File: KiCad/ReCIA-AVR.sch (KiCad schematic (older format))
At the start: 26 parts, among them U1 AVR128DA64-I_MR, U2 74AHCT1G17, U3 TLC2932AIPWR, U5 8520_DIP

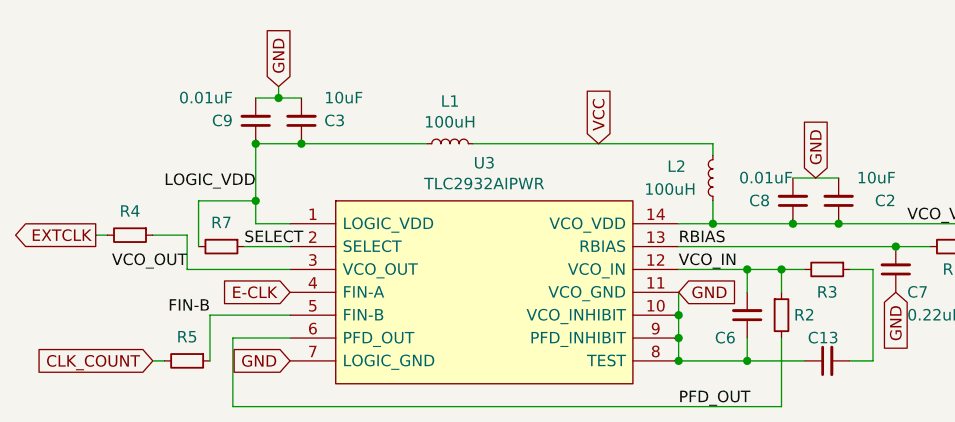
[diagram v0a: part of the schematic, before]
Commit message: corrected C8,C9 to 0.1uF
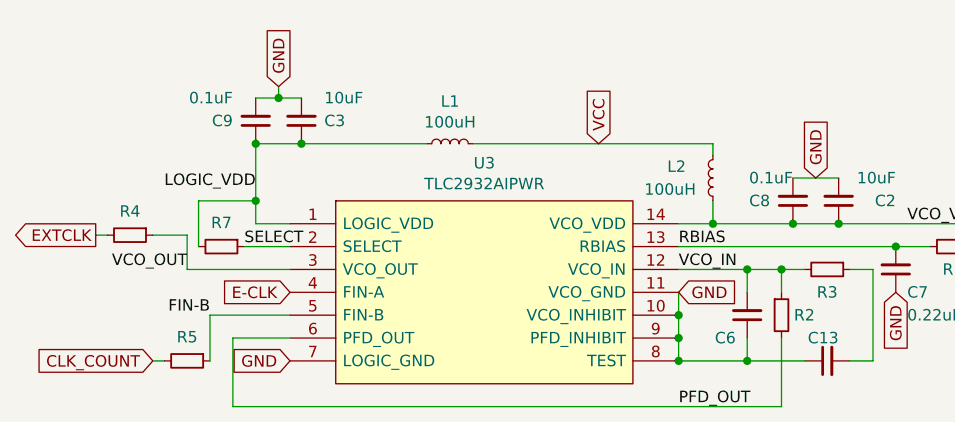
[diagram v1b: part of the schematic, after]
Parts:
- C8, C9: value 0.01uF -> 0.1uF
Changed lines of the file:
@@
 P 7650 1100
 F 0 "C9" H 7750 1100 50  0000 L CNN
-F 1 "0.01uF" H 7750 1000 50  0000 L CNN
+F 1 "0.1uF" H 7750 1000 50  0000 L CNN
 F 2 "Capacitor_SMD:C_0603_1608Metric_Pad1.08x0.95mm_HandSolder" H 7650 1100 50  0001 C CNN
 F 3 "~" H 7650 1100 50  0001 C CNN
@@
 P 10000 1450
 F 0 "C8" H 10100 1450 50  0000 L CNN
-F 1 "0.01uF" H 10000 1350 50  0000 L CNN
+F 1 "0.1uF" H 10000 1350 50  0000 L CNN
 F 2 "Capacitor_SMD:C_0603_1608Metric_Pad1.08x0.95mm_HandSolder" H 10000 1450 50  0001 C CNN
 F 3 "~" H 10000 1450 50  0001 C CNN

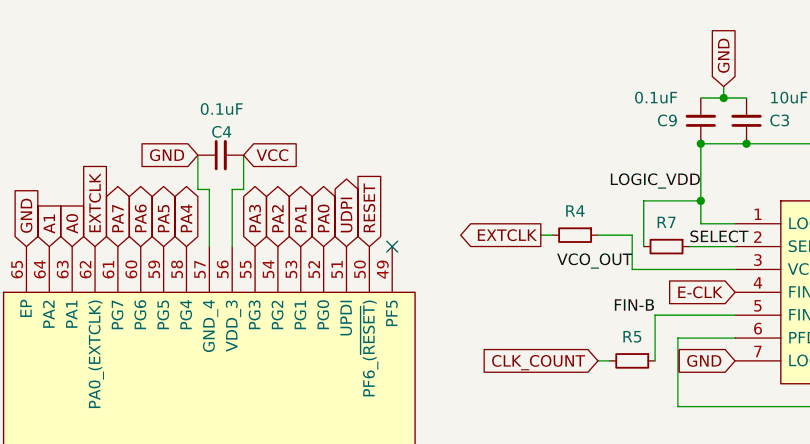
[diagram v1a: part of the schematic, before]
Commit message: Add UPDI pin-header
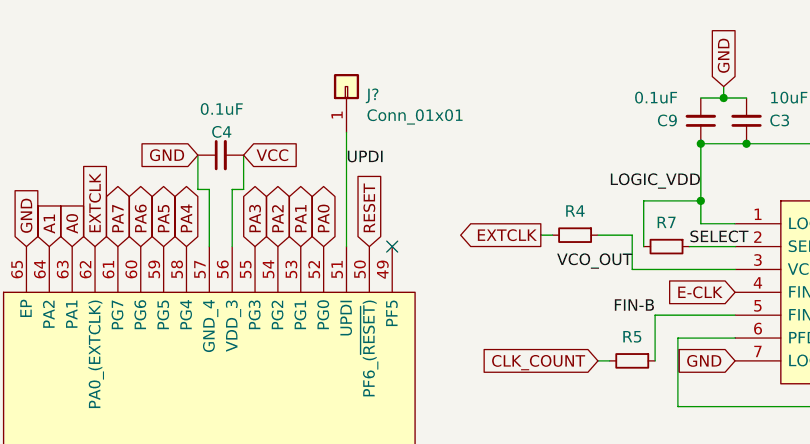
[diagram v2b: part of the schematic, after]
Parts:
- added J?: Conn_01x01, Connector_PinHeader_2.54mm:PinHeader_1x01_P2.54mm_Vertical, symbol Connector_Generic:Conn_01x01
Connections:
- net UDPI renamed UPDI
- net UPDI: now also J?.1 (Pin_1)
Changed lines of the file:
@@
 Text GLabel 4400 2750 0    50   Input ~ 0
 A3
-Text GLabel 6100 1650 1    50   BiDi ~ 0
-UDPI
 Text GLabel 5000 1650 1    50   Input ~ 0
 EXTCLK
@@
 	0    1    1    0
 $EndComp
+$Comp
+L Connector_Generic:Conn_01x01 J?
+U 1 1 679FD8AD
+P 6100 950
+F 0 "J?" V 6064 862 50  0000 R CNN
+F 1 "Conn_01x01" V 5973 862 50  0000 R CNN
+F 2 "Connector_PinHeader_2.54mm:PinHeader_1x01_P2.54mm_Vertical" H 6100 950 50  0001 C CNN
+F 3 "~" H 6100 950 50  0001 C CNN
+	1    6100 950
+	0    -1   -1   0
+$EndComp
+Wire Wire Line
+	6100 1650 6100 1150
+Text Label 6100 1300 0    50   ~ 0
+UPDI
 $EndSCHEMATC

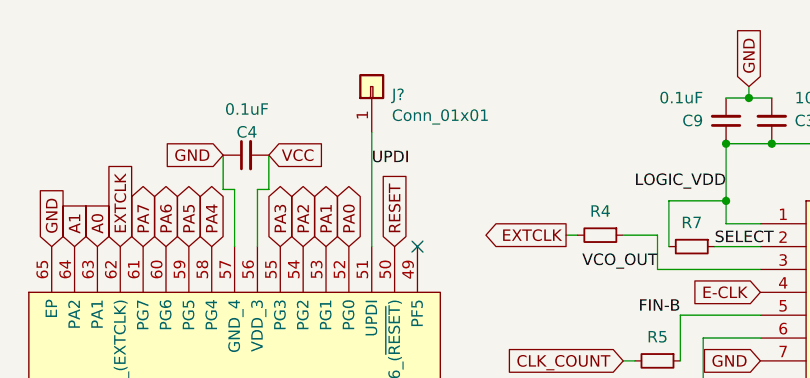
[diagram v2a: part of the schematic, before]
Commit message: Add annotation UPDI header
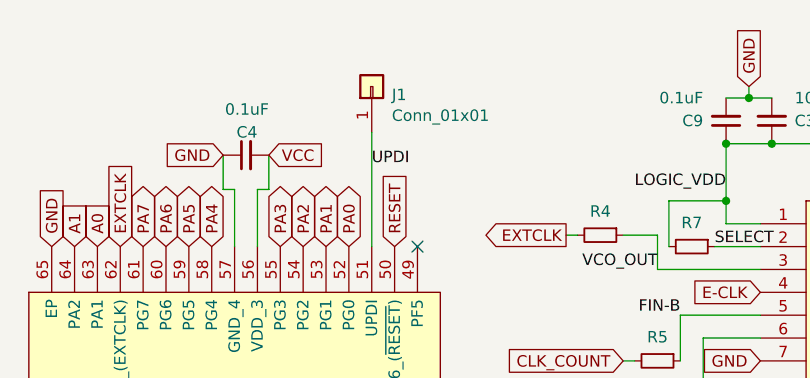
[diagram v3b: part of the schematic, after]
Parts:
- gave numbers to parts that had none: 1
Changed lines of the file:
@@
 $EndComp
 $Comp
-L Connector_Generic:Conn_01x01 J?
+L Connector_Generic:Conn_01x01 J1
 U 1 1 679FD8AD
 P 6100 950
-F 0 "J?" V 6064 862 50  0000 R CNN
+F 0 "J1" V 6064 862 50  0000 R CNN
 F 1 "Conn_01x01" V 5973 862 50  0000 R CNN
 F 2 "Connector_PinHeader_2.54mm:PinHeader_1x01_P2.54mm_Vertical" H 6100 950 50  0001 C CNN
